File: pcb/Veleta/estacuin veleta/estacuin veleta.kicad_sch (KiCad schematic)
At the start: 19 parts, among them J1 Conn_01x03, J2 Conn_01x03, J3 Conn_01x05, J4 74HC251, J5 Conn_01x09

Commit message: se readaptaron y revisaron las PCBs, listas para imprimir
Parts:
- removed J3: Conn_01x05, Connector_PinSocket_2.54mm:PinSocket_1x05_P2.54mm_Vertical, symbol Connector_Generic:Conn_01x05
- added J6: ToMother, Connector_PinSocket_2.54mm:PinSocket_1x06_P2.54mm_Vertical, symbol Connector_Generic:Conn_01x06
- J1, J2: footprint Connector_PinSocket_2.54mm:PinSocket_1x03_P2.54mm_Vertical -> Connector_PinHeader_2.54mm:PinHeader_1x03_P2.54mm_Vertical
- R1, R2, R3, R4, R5, R6, R7, R8: value R_US -> 10k; footprint Resistor_THT:R_Axial_DIN0207_L6.3mm_D2.5mm_P15.24mm_Horizontal -> Resistor_THT:R_Axial_DIN0207_L6.3mm_D2.5mm_P10.16mm_Horizontal
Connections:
- net +5V: now also J6.3 (Pin_3)
- net GND: now also R1.2, R2.2, R3.2, R4.2, R5.2, R6.2, R7.2, R8.2, J6.2 (Pin_2); no longer R1.1, R2.1, R3.1, R4.1, R5.1, R6.1, R7.1, R8.1
- net at J1.1 (Pin_1): now also J4.5 (Pin_5); no longer J4.6 (Pin_6)
- net at J1.2 (Pin_2): now also J4.6 (Pin_6)
- net at J1.3 (Pin_3): now also J6.1 (Pin_1); no longer J4.5 (Pin_5)
- net at J4.15 (Pin_15), J5.4 (Pin_4): now also R4.1; no longer R4.2
- net at J4.12 (Pin_12), J5.1 (Pin_1): now also R1.1; no longer R1.2
- net at J4.9 (Pin_9): now also J6.4 (Pin_4)
- net at J4.10 (Pin_10): now also J6.5 (Pin_5)
- net at J4.11 (Pin_11): now also J6.6 (Pin_6)
- net at J4.13 (Pin_13), J5.2 (Pin_2): now also R2.1; no longer R2.2
- net at J4.4 (Pin_4), J5.8 (Pin_8): now also R8.1; no longer R8.2
- net at J4.2 (Pin_2), J5.6 (Pin_6): now also R6.1; no longer R6.2
- net at J4.1 (Pin_1), J5.5 (Pin_5): now also R5.1; no longer R5.2
- net at J4.14 (Pin_14), J5.3 (Pin_3): now also R3.1; no longer R3.2
- net at J4.3 (Pin_3), J5.7 (Pin_7): now also R7.1; no longer R7.2
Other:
- moved on the sheet: J1

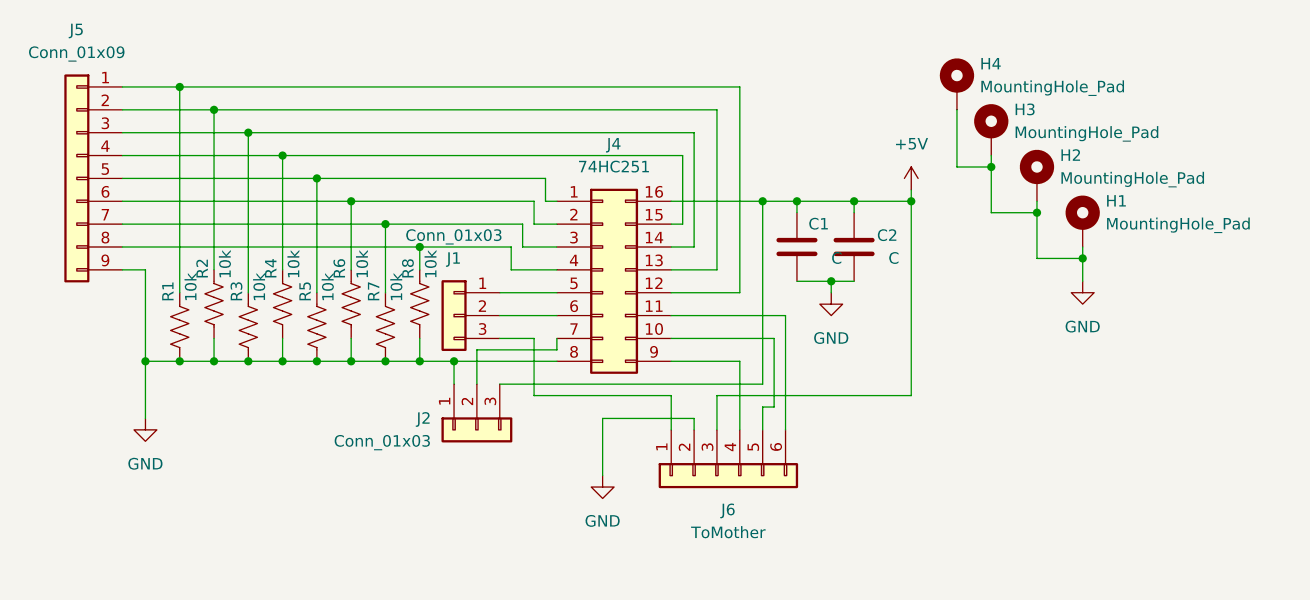
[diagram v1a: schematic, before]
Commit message: Se agregó la modificación del MQ135 a 5v con divisor resistivo; además de cambio del DHT del pin 12; también se modificaron los pines de conexión
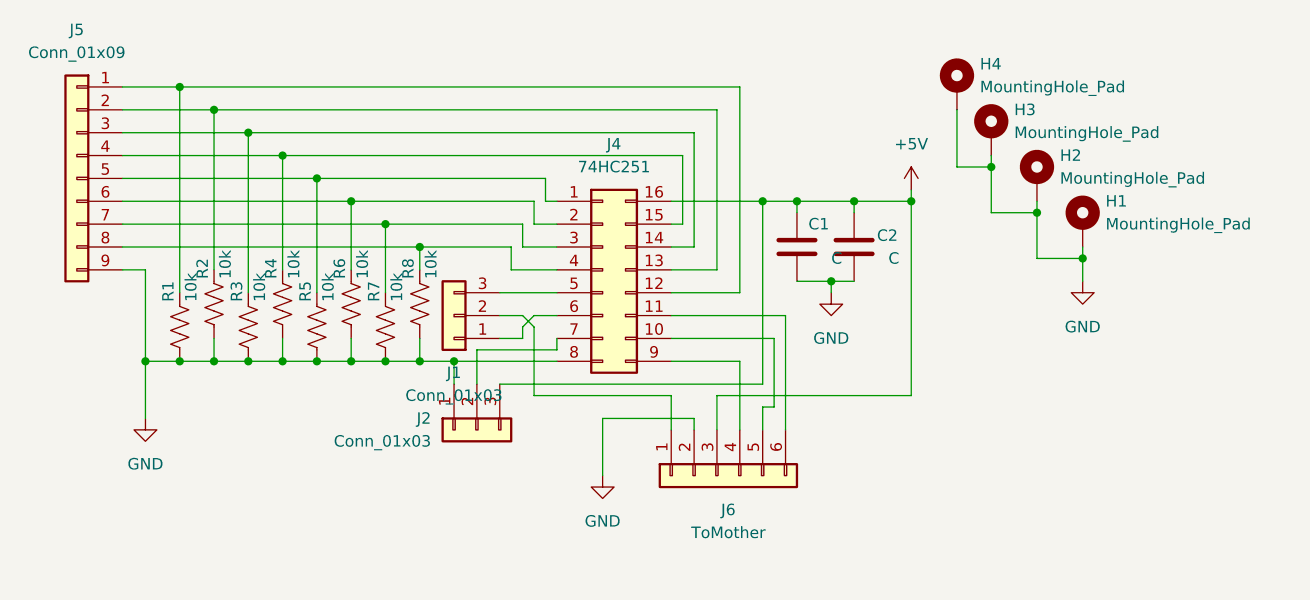
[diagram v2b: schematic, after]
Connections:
- net at J1.1 (Pin_1): now also J4.6 (Pin_6); no longer J4.5 (Pin_5)
- net at J1.2 (Pin_2): now also J6.1 (Pin_1); no longer J4.6 (Pin_6)
- net at J1.3 (Pin_3): now also J4.5 (Pin_5); no longer J6.1 (Pin_1)
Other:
- moved on the sheet: J1
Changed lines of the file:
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@@
+	(wire
+		(pts
+			(xy 69.85 45.72) (xy 68.58 46.99)
+		)
+		(stroke
+			(width 0)
+			(type default)
+		)
+	)
 	(wire
 		(pts
@@
 	(wire
 		(pts
-			(xy 66.04 48.26) (xy 69.85 48.26)
-		)
-		(stroke
-			(width 0)
-			(type default)
-		)
-	)
-	(wire
-		(pts
 			(xy 102.87 43.18) (xy 102.87 41.91)
 		)
@@
 	(wire
 		(pts
+			(xy 72.39 45.72) (xy 69.85 45.72)
+		)
+		(stroke
+			(width 0)
+			(type default)
+		)
+	)
+	(wire
+		(pts
 			(xy 34.29 22.86) (xy 34.29 40.64)
 		)
@@
 	(wire
 		(pts
+			(xy 68.58 45.72) (xy 69.85 46.99)
+		)
+		(stroke
+			(width 0)
+			(type default)
+		)
+	)
+	(wire
+		(pts
 			(xy 38.1 25.4) (xy 24.13 25.4)
 		)
@@
 	(wire
 		(pts
-			(xy 69.85 48.26) (xy 69.85 54.61)
+			(xy 69.85 46.99) (xy 69.85 54.61)
 		)
 		(stroke
@@
 	(wire
 		(pts
+			(xy 68.58 46.99) (xy 68.58 48.26)
+		)
+		(stroke
+			(width 0)
+			(type default)
+		)
+	)
+	(wire
+		(pts
 			(xy 67.31 40.64) (xy 67.31 38.1)
 		)
@@
 	(wire
 		(pts
-			(xy 66.04 45.72) (xy 72.39 45.72)
-		)
-		(stroke
-			(width 0)
-			(type default)
-		)
-	)
-	(wire
-		(pts
 			(xy 92.71 50.8) (xy 92.71 58.42)
 		)
@@
 		(pts
 			(xy 87.63 38.1) (xy 87.63 25.4)
+		)
+		(stroke
+			(width 0)
+			(type default)
+		)
+	)
+	(wire
+		(pts
+			(xy 66.04 45.72) (xy 68.58 45.72)
+		)
+		(stroke
+			(width 0)
+			(type default)
+		)
+	)
+	(wire
+		(pts
+			(xy 66.04 48.26) (xy 68.58 48.26)
 		)
 		(stroke
@@
 	(symbol
 		(lib_id "Connector_Generic:Conn_01x03")
-		(at 60.96 45.72 0)
-		(mirror y)
+		(at 60.96 45.72 180)
 		(unit 1)
 		(exclude_from_sim no)
@@
 		(dnp no)
 		(property "Reference" "J1"
-			(at 60.96 39.37 0)
+			(at 60.96 52.07 0)
 			(effects
 				(font
@@
 		)
 		(property "Value" "Conn_01x03"
-			(at 60.96 36.83 0)
+			(at 60.96 54.61 0)
 			(effects
 				(font
